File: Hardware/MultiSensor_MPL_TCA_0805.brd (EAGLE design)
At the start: 38 x 41 mm, 54 parts, among them U1 TCA9548APWR

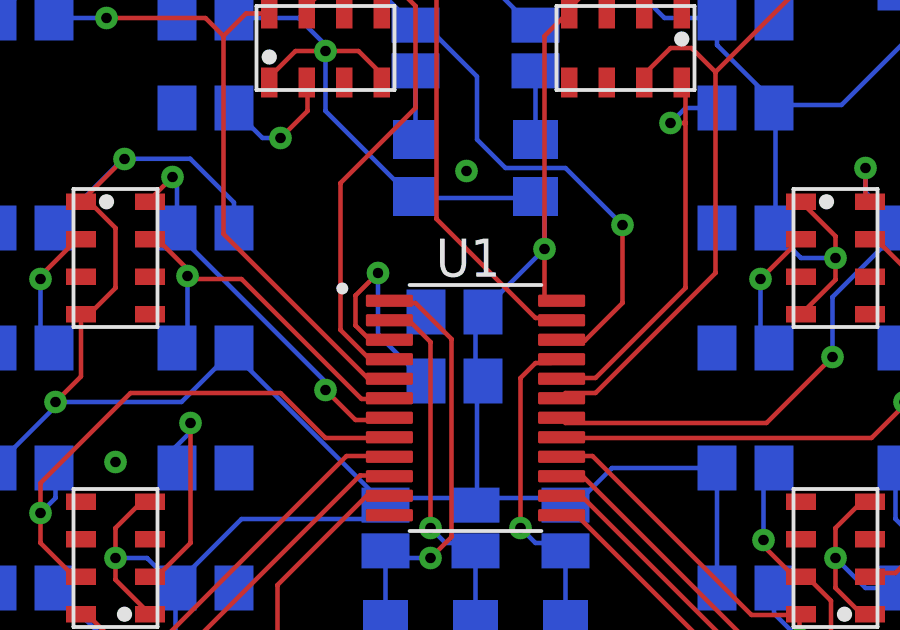
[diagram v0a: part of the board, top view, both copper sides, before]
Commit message: bulk bypass cap changed to from 0805 to 1206
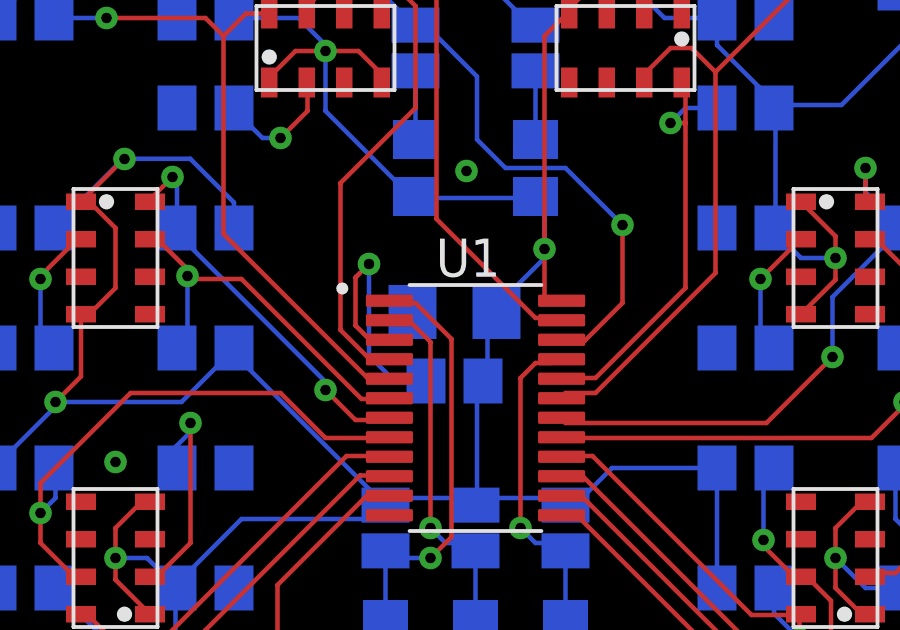
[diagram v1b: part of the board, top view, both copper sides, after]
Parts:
- C1: device rcl:C0805 -> rcl:C1206
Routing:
- net RESET: track 7.69 -> 8.88 mm
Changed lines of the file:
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@@
 <element name="B7" library="MPL115A2T1" package="MPL115A2T1" value="MPL115A2T1" x="24" y="7" smashed="yes" rot="R270"/>
 <element name="B8" library="MPL115A2T1" package="MPL115A2T1" value="MPL115A2T1" x="14" y="7" smashed="yes" rot="R90"/>
-<element name="C1" library="rcl" library_urn="urn:adsk.eagle:library:334" package="C0805" package3d_urn="urn:adsk.eagle:package:23617/2" value="10uF" x="18.3" y="22.2" smashed="yes" rot="MR0">
+<element name="C1" library="rcl" library_urn="urn:adsk.eagle:library:334" package="C1206" package3d_urn="urn:adsk.eagle:package:23618/2" value="10uF" x="18.3" y="22.2" smashed="yes" rot="MR0">
 <attribute name="NAME" x="20.53" y="22.93" size="1.27" layer="26" rot="MR180"/>
-<attribute name="POPULARITY" value="63" x="-13.45" y="18.39" size="1.778" layer="28" rot="MR0" display="off"/>
+<attribute name="POPULARITY" value="24" x="-13.45" y="18.39" size="1.778" layer="28" rot="MR0" display="off"/>
 <attribute name="SPICEPREFIX" value="C" x="-13.45" y="18.39" size="1.778" layer="28" rot="MR0" display="off"/>
 </element>
@@
 <wire x1="20.5" y1="26" x2="17" y2="26" width="0.1524" layer="16"/>
 <wire x1="21" y1="26" x2="21" y2="26.05" width="0.1524" layer="16"/>
-<wire x1="19" y1="22" x2="19" y2="19.9" width="0.1524" layer="16"/>
+<wire x1="19.4" y1="22.2" x2="19.4" y2="20.05" width="0.1524" layer="16"/>
+<wire x1="19.25" y1="19.9" x2="19.4" y2="20.05" width="0.1524" layer="16"/>
 <wire x1="19" y1="16" x2="16" y2="16" width="0.1524" layer="16"/>
 <wire x1="19" y1="16" x2="22" y2="16" width="0.1524" layer="16"/>
 <wire x1="19" y1="16" x2="19" y2="15.762" width="0.1524" layer="16"/>
-<wire x1="19" y1="19.9" x2="19.25" y2="19.9" width="0.1524" layer="16"/>
 <wire x1="22" y1="16" x2="22" y2="15.762" width="0.1524" layer="16"/>
 <wire x1="20.5" y1="26" x2="21" y2="26.05" width="0.1524" layer="16"/>
-<wire x1="19.2" y1="22.2" x2="19.25" y2="22.2" width="0.1524" layer="16"/>
+<wire x1="19.4" y1="22.2" x2="19.5" y2="22.2" width="0.1524" layer="16"/>
+<wire x1="19.5" y1="22.2" x2="19.7" y2="22.2" width="0.1524" layer="16"/>
 <wire x1="11" y1="21" x2="10.95" y2="21" width="0.1524" layer="16"/>
 <wire x1="16" y1="16" x2="16" y2="15.762" width="0.1524" layer="16"/>
@@
 <wire x1="21" y1="26.05" x2="21.3" y2="25.75" width="0.1524" layer="16"/>
 <wire x1="21.3" y1="25.75" x2="21.3" y2="24.3" width="0.1524" layer="16"/>
-<wire x1="19" y1="22" x2="19.2" y2="22.2" width="0.1524" layer="16"/>
-<wire x1="19.2" y1="22.2" x2="21.3" y2="24.3" width="0.1524" layer="16"/>
+<wire x1="21.3" y1="24" x2="19.5" y2="22.2" width="0.1524" layer="16"/>
+<wire x1="21.3" y1="24" x2="21.3" y2="24.3" width="0.1524" layer="16"/>
 <wire x1="21.3" y1="22.575" x2="21.3" y2="24.3" width="0.1524" layer="1"/>
 <wire x1="21.3" y1="31.4" x2="21.3" y2="24.3" width="0.1524" layer="1"/>
@@
 <contactref element="U1" pad="3"/>
 <contactref element="R17" pad="1"/>
-<wire x1="17.35" y1="19.9" x2="17.3" y2="19.9" width="0.1524" layer="16"/>
-<wire x1="17.3" y1="19.9" x2="15.75" y2="21.45" width="0.1524" layer="16"/>
-<wire x1="15.75" y1="23.5" x2="15.75" y2="21.45" width="0.1524" layer="16"/>
-<wire x1="15" y1="22.75" x2="15.75" y2="23.5" width="0.1524" layer="1"/>
-<wire x1="15" y1="21.75" x2="15" y2="22.75" width="0.1524" layer="1"/>
+<wire x1="17.35" y1="19.9" x2="16.3" y2="19.9" width="0.1524" layer="16"/>
+<wire x1="16.3" y1="19.9" x2="15.45" y2="20.75" width="0.1524" layer="16"/>
+<wire x1="15.45" y1="23.8" x2="15.45" y2="20.75" width="0.1524" layer="16"/>
+<wire x1="15" y1="23.35" x2="15.45" y2="23.8" width="0.1524" layer="1"/>
+<wire x1="15" y1="21.75" x2="15" y2="23.35" width="0.1524" layer="1"/>
 <wire x1="15.5" y1="21.25" x2="15" y2="21.75" width="0.1524" layer="1"/>
 <wire x1="16" y1="21.25" x2="15.5" y2="21.25" width="0.1524" layer="1"/>
 <wire x1="16" y1="21.25" x2="16.13" y2="21.275" width="0.1524" layer="1"/>
-<via x="15.75" y="23.5" extent="1-16" drill="0.35"/>
+<via x="15.45" y="23.8" extent="1-16" drill="0.35"/>
 </signal>
 <signal name="N$1">
